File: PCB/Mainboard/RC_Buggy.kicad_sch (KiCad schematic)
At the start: 12 parts, among them SW1 SW_Push, SW2 SW_Push, U1 ESP32-S3-WROOM-1

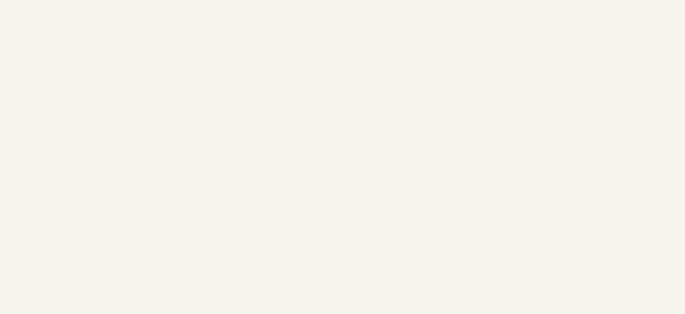
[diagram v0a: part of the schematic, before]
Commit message: Added setup, read and get Command
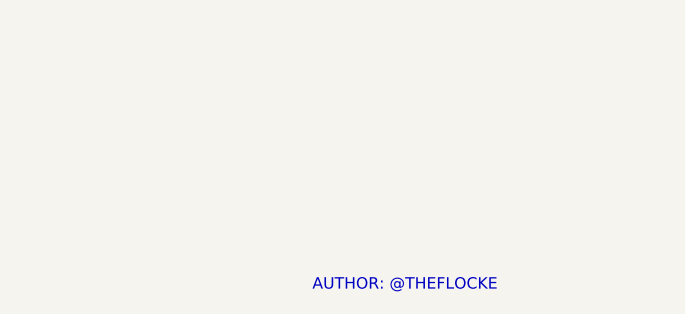
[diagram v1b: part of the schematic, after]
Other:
- note added: "AUTHOR: @THEFLOCKE"
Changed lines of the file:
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@@
+		)
+	)
+	(text "AUTHOR: @THEFLOCKE"
+		(exclude_from_sim no)
+		(at 249.936 196.596 0)
+		(effects
+			(font
+				(face "KiCad Font")
+				(size 1.27 1.27)
+				(color 194 0 194 1)
+			)
 		)
 	)

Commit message: Fixed Grammar
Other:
- removed sheet Logic Level Converter
- removed sheet PWR
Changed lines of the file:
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@@
-	)
-	(sheet
-		(at 25.4 165.1)
-		(size 38.1 25.4)
-		(exclude_from_sim no)
-		(in_bom yes)
-		(on_board yes)
-		(dnp no)
-		(stroke
-			(width 0.1524)
-			(type solid)
-		)
-		(fill
-			(color 0 0 0 0.0000)
-		)
-		(property "Sheetname" "PWR"
-			(at 25.4 164.3884 0)
-			(effects
-				(font
-					(size 1.27 1.27)
-				)
-				(justify left bottom)
-			)
-		)
-		(property "Sheetfile" "PWR.kicad_sch"
-			(at 25.4 191.77 0)
-			(effects
-				(font
-					(size 1.27 1.27)
-				)
-				(justify left top)
-			)
-		)
-		(instances
-			(project "RC_Buggy"
-				(path "/95edd31c-9fee-4eef-843b-c880bdcf4bfe"
-					(page "3")
-				)
-			)
-		)
-	)
-	(sheet
-		(at 200.66 116.84)
-		(size 67.31 26.67)
-		(exclude_from_sim no)
-		(in_bom yes)
-		(on_board yes)
-		(dnp no)
-		(stroke
-			(width 0.1524)
-			(type solid)
-		)
-		(fill
-			(color 0 0 0 0.0000)
-		)
-		(property "Sheetname" "Logic Level Converter"
-			(at 200.66 116.1284 0)
-			(effects
-				(font
-					(size 1.27 1.27)
-				)
-				(justify left bottom)
-			)
-		)
-		(property "Sheetfile" "LLC.kicad_sch"
-			(at 266.192 138.938 90)
-			(effects
-				(font
-					(size 1.27 1.27)
-				)
-				(justify left top)
-			)
-		)
-		(pin "DATA2_5V" bidirectional
-			(at 231.14 116.84 90)
-			(effects
-				(font
-					(size 1.27 1.27)
-				)
-				(justify right)
-			)
-		)
-		(pin "DATA2_3V3" bidirectional
-			(at 231.14 143.51 270)
-			(effects
-				(font
-					(size 1.27 1.27)
-				)
-				(justify left)
-			)
-		)
-		(pin "DATA0_5V" bidirectional
-			(at 226.06 116.84 90)
-			(effects
-				(font
-					(size 1.27 1.27)
-				)
-				(justify right)
-			)
-		)
-		(pin "DATA0_3V3" bidirectional
-			(at 226.06 143.51 270)
-			(effects
-				(font
-					(size 1.27 1.27)
-				)
-				(justify left)
-			)
-		)
-		(pin "DATA7_3V3" bidirectional
-			(at 243.84 143.51 270)
-			(effects
-				(font
-					(size 1.27 1.27)
-				)
-				(justify left)
-			)
-		)
-		(pin "DATA6_3V3" bidirectional
-			(at 241.3 143.51 270)
-			(effects
-				(font
-					(size 1.27 1.27)
-				)
-				(justify left)
-			)
-		)
-		(pin "DATA1_3V3" bidirectional
-			(at 228.6 143.51 270)
-			(effects
-				(font
-					(size 1.27 1.27)
-				)
-				(justify left)
-			)
-		)
-		(pin "DATA3_3V3" bidirectional
-			(at 233.68 143.51 270)
-			(effects
-				(font
-					(size 1.27 1.27)
-				)
-				(justify left)
-			)
-		)
-		(pin "DATA5_3V3" bidirectional
-			(at 238.76 143.51 270)
-			(effects
-				(font
-					(size 1.27 1.27)
-				)
-				(justify left)
-			)
-		)
-		(pin "DATA4_3V3" bidirectional
-			(at 236.22 143.51 270)
-			(effects
-				(font
-					(size 1.27 1.27)
-				)
-				(justify left)
-			)
-		)
-		(pin "DATA4_5V" bidirectional
-			(at 236.22 116.84 90)
-			(effects
-				(font
-					(size 1.27 1.27)
-				)
-				(justify right)
-			)
-		)
-		(pin "DATA7_5V" bidirectional
-			(at 243.84 116.84 90)
-			(effects
-				(font
-					(size 1.27 1.27)
-				)
-				(justify right)
-			)
-		)
-		(pin "DATA6_5V" bidirectional
-			(at 241.3 116.84 90)
-			(effects
-				(font
-					(size 1.27 1.27)
-				)
-				(justify right)
-			)
-		)
-		(pin "DATA1_5V" bidirectional
-			(at 228.6 116.84 90)
-			(effects
-				(font
-					(size 1.27 1.27)
-				)
-				(justify right)
-			)
-		)
-		(pin "DATA3_5V" bidirectional
-			(at 233.68 116.84 90)
-			(effects
-				(font
-					(size 1.27 1.27)
-				)
-				(justify right)
-			)
-		)
-		(pin "DATA5_5V" bidirectional
-			(at 238.76 116.84 90)
-			(effects
-				(font
-					(size 1.27 1.27)
-				)
-				(justify right)
-			)
-		)
-		(instances
-			(project "RC_Buggy"
-				(path "/95edd31c-9fee-4eef-843b-c880bdcf4bfe"
-					(page "4")
-				)
-			)
-		)
 	)
 	(sheet

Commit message: upload images and deleted pcb new
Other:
- added sheet Logic Level Converter (LLC.kicad_sch)
- added sheet PWR (PWR.kicad_sch)
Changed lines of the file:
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@@
+	)
+	(sheet
+		(at 25.4 165.1)
+		(size 38.1 25.4)
+		(exclude_from_sim no)
+		(in_bom yes)
+		(on_board yes)
+		(dnp no)
+		(stroke
+			(width 0.1524)
+			(type solid)
+		)
+		(fill
+			(color 0 0 0 0.0000)
+		)
+		(property "Sheetname" "PWR"
+			(at 25.4 164.3884 0)
+			(effects
+				(font
+					(size 1.27 1.27)
+				)
+				(justify left bottom)
+			)
+		)
+		(property "Sheetfile" "PWR.kicad_sch"
+			(at 25.4 191.77 0)
+			(effects
+				(font
+					(size 1.27 1.27)
+				)
+				(justify left top)
+			)
+		)
+		(instances
+			(project "RC_Buggy"
+				(path "/95edd31c-9fee-4eef-843b-c880bdcf4bfe"
+					(page "3")
+				)
+			)
+		)
+	)
+	(sheet
+		(at 200.66 116.84)
+		(size 67.31 26.67)
+		(exclude_from_sim no)
+		(in_bom yes)
+		(on_board yes)
+		(dnp no)
+		(stroke
+			(width 0.1524)
+			(type solid)
+		)
+		(fill
+			(color 0 0 0 0.0000)
+		)
+		(property "Sheetname" "Logic Level Converter"
+			(at 200.66 116.1284 0)
+			(effects
+				(font
+					(size 1.27 1.27)
+				)
+				(justify left bottom)
+			)
+		)
+		(property "Sheetfile" "LLC.kicad_sch"
+			(at 266.192 138.938 90)
+			(effects
+				(font
+					(size 1.27 1.27)
+				)
+				(justify left top)
+			)
+		)
+		(pin "DATA2_5V" bidirectional
+			(at 231.14 116.84 90)
+			(effects
+				(font
+					(size 1.27 1.27)
+				)
+				(justify right)
+			)
+		)
+		(pin "DATA2_3V3" bidirectional
+			(at 231.14 143.51 270)
+			(effects
+				(font
+					(size 1.27 1.27)
+				)
+				(justify left)
+			)
+		)
+		(pin "DATA0_5V" bidirectional
+			(at 226.06 116.84 90)
+			(effects
+				(font
+					(size 1.27 1.27)
+				)
+				(justify right)
+			)
+		)
+		(pin "DATA0_3V3" bidirectional
+			(at 226.06 143.51 270)
+			(effects
+				(font
+					(size 1.27 1.27)
+				)
+				(justify left)
+			)
+		)
+		(pin "DATA7_3V3" bidirectional
+			(at 243.84 143.51 270)
+			(effects
+				(font
+					(size 1.27 1.27)
+				)
+				(justify left)
+			)
+		)
+		(pin "DATA6_3V3" bidirectional
+			(at 241.3 143.51 270)
+			(effects
+				(font
+					(size 1.27 1.27)
+				)
+				(justify left)
+			)
+		)
+		(pin "DATA1_3V3" bidirectional
+			(at 228.6 143.51 270)
+			(effects
+				(font
+					(size 1.27 1.27)
+				)
+				(justify left)
+			)
+		)
+		(pin "DATA3_3V3" bidirectional
+			(at 233.68 143.51 270)
+			(effects
+				(font
+					(size 1.27 1.27)
+				)
+				(justify left)
+			)
+		)
+		(pin "DATA5_3V3" bidirectional
+			(at 238.76 143.51 270)
+			(effects
+				(font
+					(size 1.27 1.27)
+				)
+				(justify left)
+			)
+		)
+		(pin "DATA4_3V3" bidirectional
+			(at 236.22 143.51 270)
+			(effects
+				(font
+					(size 1.27 1.27)
+				)
+				(justify left)
+			)
+		)
+		(pin "DATA4_5V" bidirectional
+			(at 236.22 116.84 90)
+			(effects
+				(font
+					(size 1.27 1.27)
+				)
+				(justify right)
+			)
+		)
+		(pin "DATA7_5V" bidirectional
+			(at 243.84 116.84 90)
+			(effects
+				(font
+					(size 1.27 1.27)
+				)
+				(justify right)
+			)
+		)
+		(pin "DATA6_5V" bidirectional
+			(at 241.3 116.84 90)
+			(effects
+				(font
+					(size 1.27 1.27)
+				)
+				(justify right)
+			)
+		)
+		(pin "DATA1_5V" bidirectional
+			(at 228.6 116.84 90)
+			(effects
+				(font
+					(size 1.27 1.27)
+				)
+				(justify right)
+			)
+		)
+		(pin "DATA3_5V" bidirectional
+			(at 233.68 116.84 90)
+			(effects
+				(font
+					(size 1.27 1.27)
+				)
+				(justify right)
+			)
+		)
+		(pin "DATA5_5V" bidirectional
+			(at 238.76 116.84 90)
+			(effects
+				(font
+					(size 1.27 1.27)
+				)
+				(justify right)
+			)
+		)
+		(instances
+			(project "RC_Buggy"
+				(path "/95edd31c-9fee-4eef-843b-c880bdcf4bfe"
+					(page "4")
+				)
+			)
+		)
 	)
 	(sheet
